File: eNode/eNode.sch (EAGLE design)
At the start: 33 parts, among them IC1 MCP1700-33, IC2 MCP73831/OT

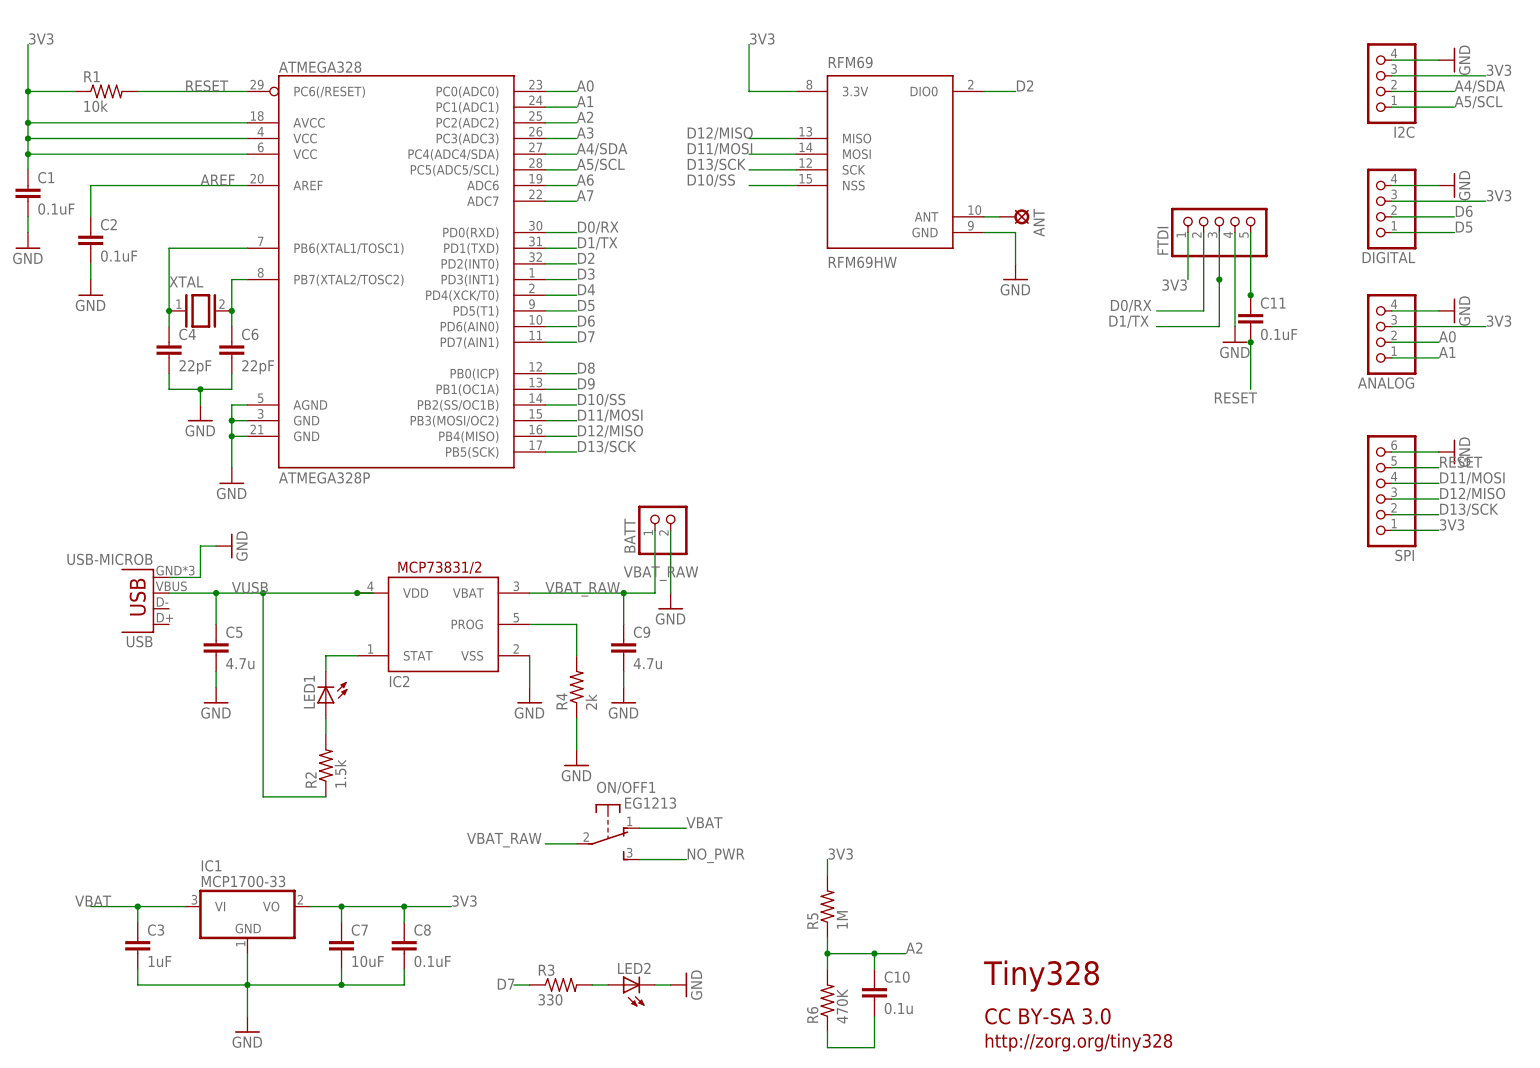
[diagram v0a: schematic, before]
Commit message: Update eNode board and schematic
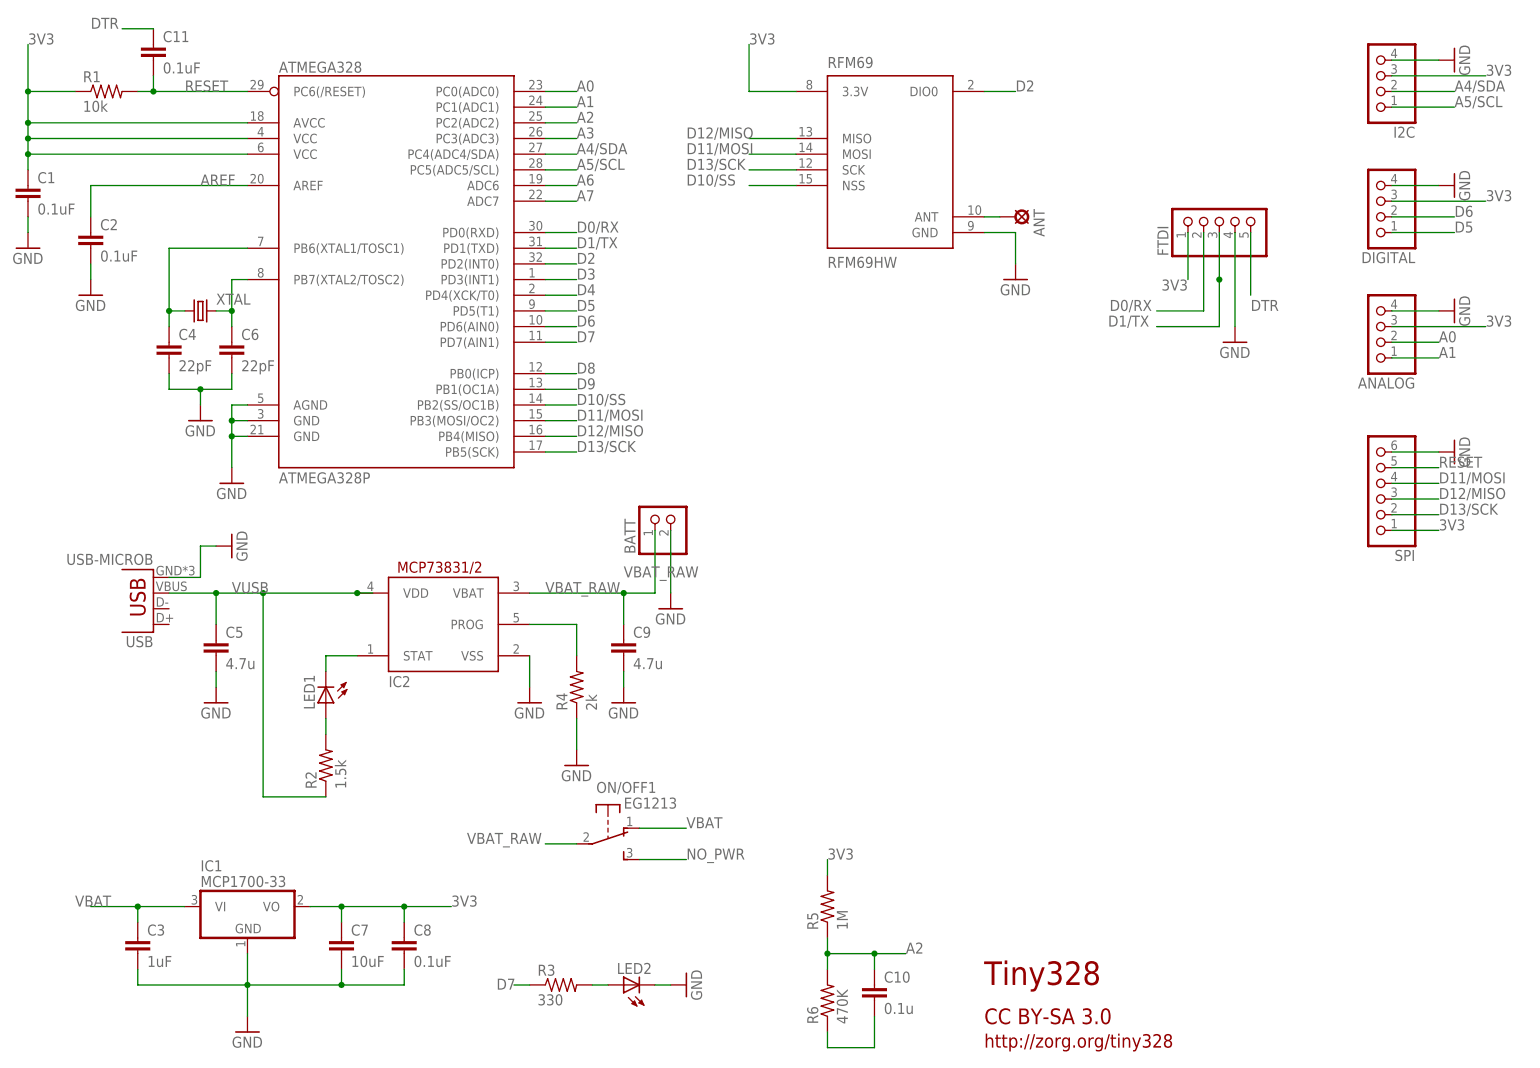
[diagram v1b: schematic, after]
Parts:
- XTAL: device special:XTAL/S -> SparkFun-FreqCtrl:CRYSTALSMD
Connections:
- new net DTR: C11.1, FTDI.5
- net RESET: no longer C11.1, FTDI.5
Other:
- moved on the sheet: C11
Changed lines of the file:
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@@
 <layer number="251" name="SMDround" color="12" fill="11" visible="no" active="no"/>
 <layer number="254" name="cooling" color="7" fill="1" visible="no" active="yes"/>
+<layer number="255" name="routoute" color="7" fill="1" visible="yes" active="yes"/>
 </layers>
 <schematic xreflabel="%F%N/%S.%C%R" xrefpart="/%S.%C%R">
@@
 <part name="SPI" library="pinhead" deviceset="PINHD-1X6" device=""/>
 <part name="GND18" library="supply1" deviceset="GND" device=""/>
-<part name="XTAL" library="special" deviceset="XTAL/S" device=""/>
 <part name="USB" library="SparkFun-Connectors" deviceset="USB" device="-MICROB"/>
 <part name="GND6" library="supply1" deviceset="GND" device=""/>
@@
 <part name="C4" library="SparkFun-Passives" deviceset="CAP" device="0603-CAP" value="22pF"/>
 <part name="C6" library="SparkFun-Passives" deviceset="CAP" device="0603-CAP" value="22pF"/>
+<part name="XTAL" library="SparkFun-FreqCtrl" deviceset="CRYSTAL" device="SMD"/>
 </parts>
 <sheets>
@@
 <instance part="FTDI" gate="A" x="63.5" y="73.66" rot="R90"/>
 <instance part="GND14" gate="1" x="66.04" y="53.34"/>
-<instance part="C11" gate="G$1" x="68.58" y="55.88"/>
+<instance part="C11" gate="G$1" x="-109.22" y="99.06"/>
 <instance part="I2C" gate="A" x="88.9" y="96.52" rot="R180"/>
 <instance part="DIGITAL" gate="A" x="88.9" y="76.2" rot="R180"/>
@@
 <instance part="SPI" gate="A" x="88.9" y="30.48" rot="R180"/>
 <instance part="GND18" gate="1" x="101.6" y="35.56" rot="R90"/>
-<instance part="XTAL" gate="G$1" x="-101.6" y="58.42"/>
 <instance part="USB" gate="G$1" x="-109.22" y="15.24" rot="R180"/>
 <instance part="GND6" gate="1" x="-96.52" y="20.32" rot="R90"/>
@@
 <instance part="C4" gate="G$1" x="-106.68" y="50.8"/>
 <instance part="C6" gate="G$1" x="-96.52" y="50.8"/>
+<instance part="XTAL" gate="G$1" x="-101.6" y="58.42"/>
 </instances>
 <busses>
@@
 <pinref part="ATMEGA328P" gate="G$1" pin="PC6(/RESET)"/>
 <pinref part="R1" gate="G$1" pin="2"/>
-<wire x1="-93.98" y1="93.98" x2="-111.76" y2="93.98" width="0.1524" layer="91"/>
+<wire x1="-93.98" y1="93.98" x2="-109.22" y2="93.98" width="0.1524" layer="91"/>
 <label x="-104.14" y="93.98" size="1.778" layer="95"/>
-</segment>
-<segment>
-<wire x1="68.58" y1="45.72" x2="68.58" y2="53.34" width="0.1524" layer="91"/>
-<label x="69.596" y="45.212" size="1.778" layer="95" rot="R180"/>
+<wire x1="-109.22" y1="93.98" x2="-111.76" y2="93.98" width="0.1524" layer="91"/>
+<wire x1="-109.22" y1="93.98" x2="-109.22" y2="96.52" width="0.1524" layer="91"/>
+<junction x="-109.22" y="93.98"/>
 <pinref part="C11" gate="G$1" pin="2"/>
-<junction x="68.58" y="53.34"/>
 </segment>
 <segment>
@@
 <wire x1="91.44" y1="33.02" x2="99.06" y2="33.02" width="0.1524" layer="91"/>
 <label x="99.06" y="33.02" size="1.778" layer="95"/>
-</segment>
-<segment>
-<pinref part="FTDI" gate="A" pin="5"/>
-<wire x1="68.58" y1="71.12" x2="68.58" y2="60.96" width="0.1524" layer="91"/>
-<pinref part="C11" gate="G$1" pin="1"/>
-<junction x="68.58" y="60.96"/>
 </segment>
 </net>
@@
 <net name="N$3" class="0">
 <segment>
-<pinref part="XTAL" gate="G$1" pin="1"/>
 <wire x1="-106.68" y1="68.58" x2="-106.68" y2="58.42" width="0.1524" layer="91"/>
 <pinref part="ATMEGA328P" gate="G$1" pin="PB6(XTAL1/TOSC1)"/>
+<wire x1="-106.68" y1="58.42" x2="-106.68" y2="55.88" width="0.1524" layer="91"/>
 <wire x1="-93.98" y1="68.58" x2="-106.68" y2="68.58" width="0.1524" layer="91"/>
-<wire x1="-106.68" y1="58.42" x2="-106.68" y2="55.88" width="0.1524" layer="91"/>
+<pinref part="C4" gate="G$1" pin="1"/>
+<wire x1="-104.14" y1="58.42" x2="-106.68" y2="58.42" width="0.1524" layer="91"/>
 <junction x="-106.68" y="58.42"/>
-<pinref part="C4" gate="G$1" pin="1"/>
+<pinref part="XTAL" gate="G$1" pin="1"/>
 </segment>
 </net>
 <net name="N$4" class="0">
 <segment>
-<pinref part="XTAL" gate="G$1" pin="2"/>
 <wire x1="-96.52" y1="63.5" x2="-96.52" y2="58.42" width="0.1524" layer="91"/>
 <pinref part="ATMEGA328P" gate="G$1" pin="PB7(XTAL2/TOSC2)"/>
+<wire x1="-96.52" y1="58.42" x2="-96.52" y2="55.88" width="0.1524" layer="91"/>
 <wire x1="-93.98" y1="63.5" x2="-96.52" y2="63.5" width="0.1524" layer="91"/>
-<wire x1="-96.52" y1="55.88" x2="-96.52" y2="58.42" width="0.1524" layer="91"/>
+<pinref part="C6" gate="G$1" pin="1"/>
+<wire x1="-99.06" y1="58.42" x2="-96.52" y2="58.42" width="0.1524" layer="91"/>
 <junction x="-96.52" y="58.42"/>
-<pinref part="C6" gate="G$1" pin="1"/>
+<pinref part="XTAL" gate="G$1" pin="2"/>
 </segment>
 </net>
@@
 </segment>
 </net>
+<net name="DTR" class="0">
+<segment>
+<pinref part="C11" gate="G$1" pin="1"/>
+<wire x1="-109.22" y1="104.14" x2="-114.3" y2="104.14" width="0.1524" layer="91"/>
+<label x="-119.38" y="104.14" size="1.778" layer="95"/>
+</segment>
+<segment>
+<pinref part="FTDI" gate="A" pin="5"/>
+<wire x1="68.58" y1="71.12" x2="68.58" y2="60.96" width="0.1524" layer="91"/>
+<label x="68.58" y="58.42" size="1.778" layer="95"/>
+</segment>
+</net>

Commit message: Update final eNode version 1
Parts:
- removed C4, C6: 22pF, SparkFun-Passives:CAP0603-CAP
- removed XTAL: (no value), SparkFun-FreqCtrl:CRYSTALSMD
- added X1: 16MHZ, SparkFun-FreqCtrl:RESONATOR16MHZ
- R3: value 330 -> 1K
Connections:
- net N$5 renamed STAT
- net N$7 renamed PROG
- net GND: now also X1.2; no longer C4.2, C6.2
- net N$3: now also X1.1; no longer C4.1, XTAL.1
- net N$4: now also X1.3; no longer C6.1, XTAL.2
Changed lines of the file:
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@@
 <part name="C2" library="SparkFun-Passives" deviceset="CAP" device="0603-CAP" value="0.1uF"/>
 <part name="R1" library="SparkFun-Passives" deviceset="RESISTOR" device="0603-RES" value="10k"/>
-<part name="GND3" library="supply1" deviceset="GND" device=""/>
 <part name="GND5" library="supply1" deviceset="GND" device=""/>
 <part name="GND2" library="supply1" deviceset="GND" device=""/>
@@
 <part name="RFM69" library="SparkFun-RF" deviceset="RFM69H" device="W"/>
 <part name="GND13" library="supply1" deviceset="GND" device=""/>
-<part name="R3" library="SparkFun-Passives" deviceset="RESISTOR" device="0603-RES" value="330"/>
+<part name="R3" library="SparkFun-Passives" deviceset="RESISTOR" device="0603-RES" value="1K"/>
 <part name="LED2" library="adafruit" deviceset="LED" device="CHIPLED_0603"/>
 <part name="GND12" library="supply1" deviceset="GND" device=""/>
@@
 <part name="GND6" library="supply1" deviceset="GND" device=""/>
 <part name="ON/OFF" library="adafruit" deviceset="EG1213" device=""/>
-<part name="C4" library="SparkFun-Passives" deviceset="CAP" device="0603-CAP" value="22pF"/>
-<part name="C6" library="SparkFun-Passives" deviceset="CAP" device="0603-CAP" value="22pF"/>
-<part name="XTAL" library="SparkFun-FreqCtrl" deviceset="CRYSTAL" device="SMD"/>
+<part name="X1" library="SparkFun-FreqCtrl" deviceset="RESONATOR" device="16MHZ" value="16MHZ"/>
 </parts>
 <sheets>
@@
 <instance part="C2" gate="G$1" x="-119.38" y="68.58"/>
 <instance part="R1" gate="G$1" x="-116.84" y="93.98"/>
-<instance part="GND3" gate="1" x="-101.6" y="40.64"/>
 <instance part="GND5" gate="1" x="-96.52" y="30.48"/>
 <instance part="GND2" gate="1" x="-119.38" y="60.96"/>
@@
 <instance part="GND6" gate="1" x="-96.52" y="20.32" rot="R90"/>
 <instance part="ON/OFF" gate="1" x="-35.56" y="-27.94" rot="R270"/>
-<instance part="C4" gate="G$1" x="-106.68" y="50.8"/>
-<instance part="C6" gate="G$1" x="-96.52" y="50.8"/>
-<instance part="XTAL" gate="G$1" x="-101.6" y="58.42"/>
+<instance part="X1" gate="G$1" x="-96.52" y="55.88" smashed="yes">
+<attribute name="NAME" x="-93.98" y="59.944" size="1.778" layer="95" rot="R180"/>
+<attribute name="VALUE" x="-93.98" y="48.26" size="1.778" layer="96"/>
+</instance>
 </instances>
 <busses>
@@
 <net name="GND" class="0">
 <segment>
-<pinref part="ATMEGA328P" gate="G$1" pin="AGND"/>
-<wire x1="-93.98" y1="43.18" x2="-96.52" y2="43.18" width="0.1524" layer="91"/>
 <pinref part="GND5" gate="1" pin="GND"/>
+<wire x1="-96.52" y1="48.26" x2="-96.52" y2="43.18" width="0.1524" layer="91"/>
+<pinref part="ATMEGA328P" gate="G$1" pin="GND@1"/>
 <wire x1="-96.52" y1="43.18" x2="-96.52" y2="40.64" width="0.1524" layer="91"/>
-<pinref part="ATMEGA328P" gate="G$1" pin="GND@1"/>
 <wire x1="-96.52" y1="40.64" x2="-96.52" y2="38.1" width="0.1524" layer="91"/>
 <wire x1="-96.52" y1="38.1" x2="-96.52" y2="33.02" width="0.1524" layer="91"/>
@@
 <wire x1="-93.98" y1="38.1" x2="-96.52" y2="38.1" width="0.1524" layer="91"/>
 <junction x="-96.52" y="38.1"/>
+<pinref part="X1" gate="G$1" pin="2"/>
+<pinref part="ATMEGA328P" gate="G$1" pin="AGND"/>
+<wire x1="-93.98" y1="43.18" x2="-96.52" y2="43.18" width="0.1524" layer="91"/>
+<junction x="-96.52" y="43.18"/>
 </segment>
 <segment>
@@
 <wire x1="91.44" y1="35.56" x2="99.06" y2="35.56" width="0.1524" layer="91"/>
 <pinref part="GND18" gate="1" pin="GND"/>
-</segment>
-<segment>
-<wire x1="-106.68" y1="45.72" x2="-101.6" y2="45.72" width="0.1524" layer="91"/>
-<wire x1="-101.6" y1="45.72" x2="-101.6" y2="43.18" width="0.1524" layer="91"/>
-<wire x1="-96.52" y1="45.72" x2="-101.6" y2="45.72" width="0.1524" layer="91"/>
-<junction x="-101.6" y="45.72"/>
-<pinref part="GND3" gate="1" pin="GND"/>
-<wire x1="-106.68" y1="48.26" x2="-106.68" y2="45.72" width="0.1524" layer="91"/>
-<wire x1="-96.52" y1="45.72" x2="-96.52" y2="48.26" width="0.1524" layer="91"/>
-<pinref part="C4" gate="G$1" pin="2"/>
-<pinref part="C6" gate="G$1" pin="2"/>
 </segment>
 <segment>
@@
 </segment>
 </net>
-<net name="N$5" class="0">
+<net name="STAT" class="0">
 <segment>
 <pinref part="LED1" gate="G$1" pin="C"/>
@@
 </segment>
 </net>
-<net name="N$7" class="0">
+<net name="PROG" class="0">
 <segment>
 <pinref part="IC2" gate="G$1" pin="PROG"/>
@@
 <net name="N$3" class="0">
 <segment>
-<wire x1="-106.68" y1="68.58" x2="-106.68" y2="58.42" width="0.1524" layer="91"/>
+<wire x1="-99.06" y1="68.58" x2="-99.06" y2="55.88" width="0.1524" layer="91"/>
 <pinref part="ATMEGA328P" gate="G$1" pin="PB6(XTAL1/TOSC1)"/>
-<wire x1="-106.68" y1="58.42" x2="-106.68" y2="55.88" width="0.1524" layer="91"/>
-<wire x1="-93.98" y1="68.58" x2="-106.68" y2="68.58" width="0.1524" layer="91"/>
-<pinref part="C4" gate="G$1" pin="1"/>
-<wire x1="-104.14" y1="58.42" x2="-106.68" y2="58.42" width="0.1524" layer="91"/>
-<junction x="-106.68" y="58.42"/>
-<pinref part="XTAL" gate="G$1" pin="1"/>
+<wire x1="-99.06" y1="55.88" x2="-99.06" y2="50.8" width="0.1524" layer="91"/>
+<wire x1="-93.98" y1="68.58" x2="-99.06" y2="68.58" width="0.1524" layer="91"/>
+<pinref part="X1" gate="G$1" pin="1"/>
+<junction x="-99.06" y="55.88"/>
 </segment>
 </net>
 <net name="N$4" class="0">
 <segment>
-<wire x1="-96.52" y1="63.5" x2="-96.52" y2="58.42" width="0.1524" layer="91"/>
+<wire x1="-93.98" y1="63.5" x2="-93.98" y2="55.88" width="0.1524" layer="91"/>
 <pinref part="ATMEGA328P" gate="G$1" pin="PB7(XTAL2/TOSC2)"/>
-<wire x1="-96.52" y1="58.42" x2="-96.52" y2="55.88" width="0.1524" layer="91"/>
-<wire x1="-93.98" y1="63.5" x2="-96.52" y2="63.5" width="0.1524" layer="91"/>
-<pinref part="C6" gate="G$1" pin="1"/>
-<wire x1="-99.06" y1="58.42" x2="-96.52" y2="58.42" width="0.1524" layer="91"/>
-<junction x="-96.52" y="58.42"/>
-<pinref part="XTAL" gate="G$1" pin="2"/>
-</segment>
-</net>
+<pinref part="X1" gate="G$1" pin="3"/>
+<wire x1="-93.98" y1="55.88" x2="-93.98" y2="50.8" width="0.1524" layer="91"/>
+<junction x="-93.98" y="55.88"/>
+</segment>
+</net>
